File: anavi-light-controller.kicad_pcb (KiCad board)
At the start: 2 copper layers, 74.9 x 40.6 mm, 23 parts, among them J1 Screw_Terminal_1x04, P1 CONN_01X03, Q1 IRF8721PBF-1, Q2 IRF8721PBF-1, Q3 IRF8721PBF-1, SW1 SW_DIP_x01, U1 I2C_SENS_1, U2 I2C_SENS_1, U3 I2C_SENS_1

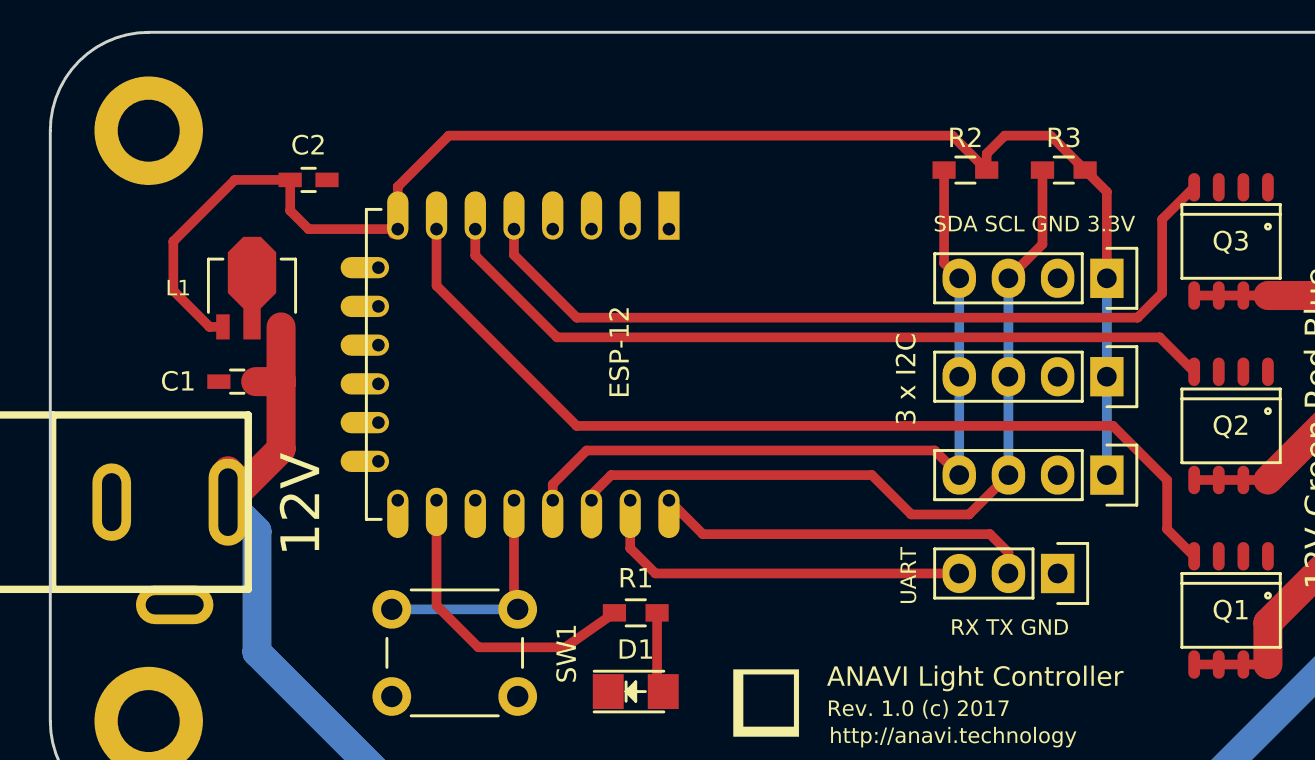
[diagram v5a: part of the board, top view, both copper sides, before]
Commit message: Change LDO voltage regulator
Use LD1117S33TR as LDO voltage regulator to drop
from 12V to 3.3V and to power the ESP8266 module.

Signed-off-by: Leon Anavi <leon@anavi.org>
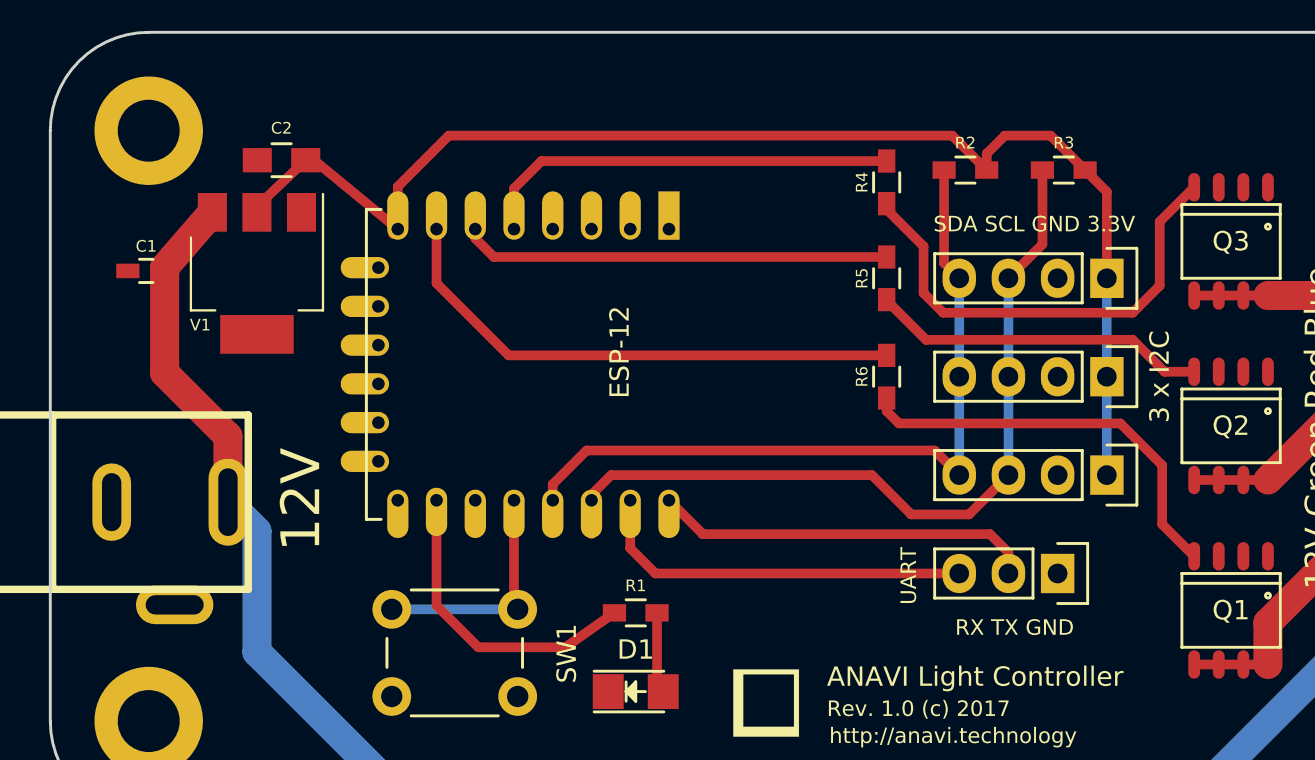
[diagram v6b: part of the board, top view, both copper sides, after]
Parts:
- removed L1: 78L33, smd-semi:SOT-89
- added R4: 220R, Resistors_SMD:R_0603_HandSoldering, F.Cu at (108.0, 78.9)
- added R5: 220R, Resistors_SMD:R_0603_HandSoldering, F.Cu at (108.0, 83.8)
- added R6: 220R, Resistors_SMD:R_0603_HandSoldering, F.Cu at (108.0, 88.9)
- added V1: LD1117S33TR, SOT-223, F.Cu at (75.4, 83.6)
- C1: value C -> 100nF
- C2: value C -> 10uF; footprint Capacitors_SMD:C_0603_HandSoldering -> Capacitors_SMD:C_0805_HandSoldering
- DC1: value 12V -> dc_jack
- moved C1 7.40 mm to (69.7, 83.4)
- moved C2 1.73 mm to (76.7, 77.7), turned to 180 degrees
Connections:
- Q1 pad 4: Net-(ESP-12-Pad7) -> Net-(Q1-Pad4)
- Q2 pad 4: Net-(ESP-12-Pad6) -> Net-(Q2-Pad4)
- Q3 pad 4: Net-(ESP-12-Pad5) -> Net-(Q3-Pad4)
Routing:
- net Net-(Q3-Pad4): track 0.00 -> 24.9 mm
- net Net-(Q1-Pad4): track 0.00 -> 21.9 mm
- net Net-(ESP-12-Pad7): track 49.3 -> 27.6 mm
- net Net-(ESP-12-Pad5): track 43.3 -> 21.9 mm
- net Net-(ESP-12-Pad6): track 41.1 -> 22.2 mm
- net Net-(Q2-Pad4): track 0.00 -> 17.6 mm
- net +3V3: track 79.3 -> 69.5 mm
- net +12V: track 91.6 -> 95.7 mm
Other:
- board text added: "12V"

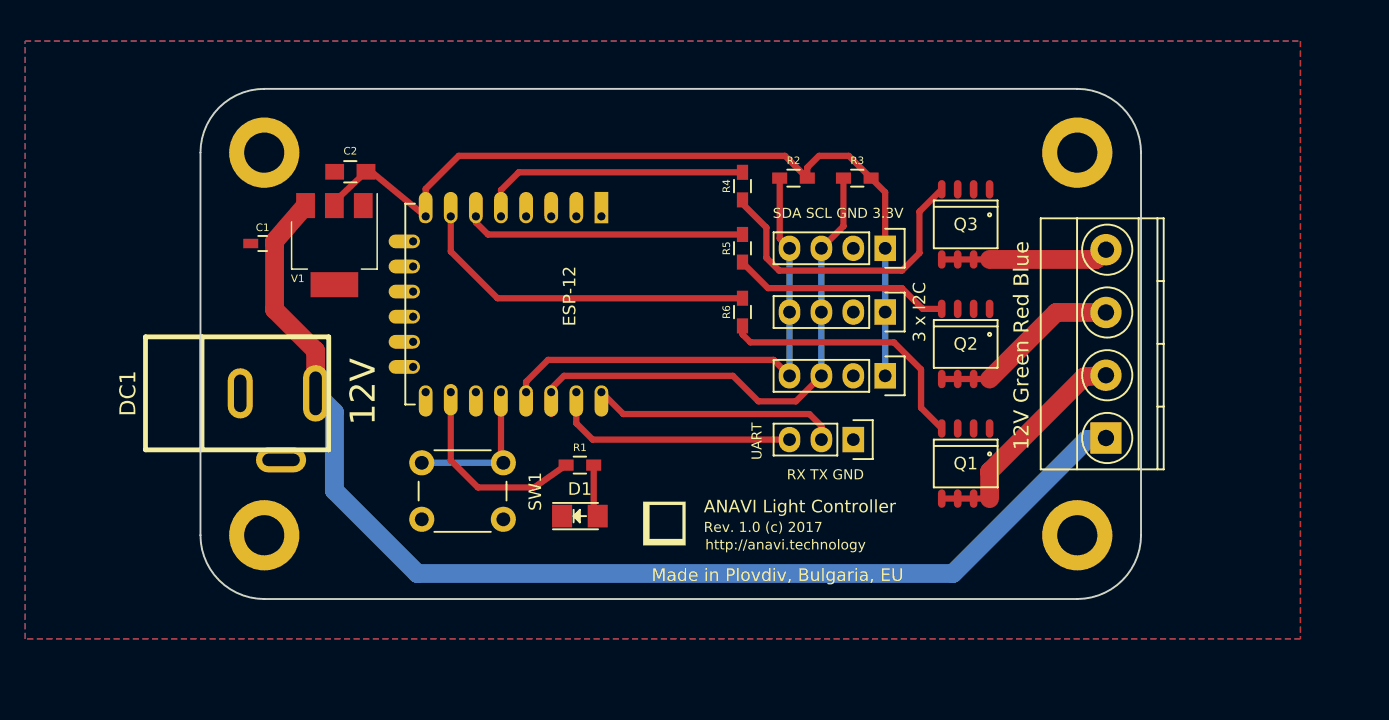
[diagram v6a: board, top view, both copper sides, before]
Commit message: Enable ESP-12; Fix the button and LED
Enable ESP-12 by connecting GPIO5 to GND and CH_PD
to 3.3V. Add 2K resistor to GPIO0 to fix the button
and move the alarm LED on the other side.

Signed-off-by: Leon Anavi <leon@anavi.org>
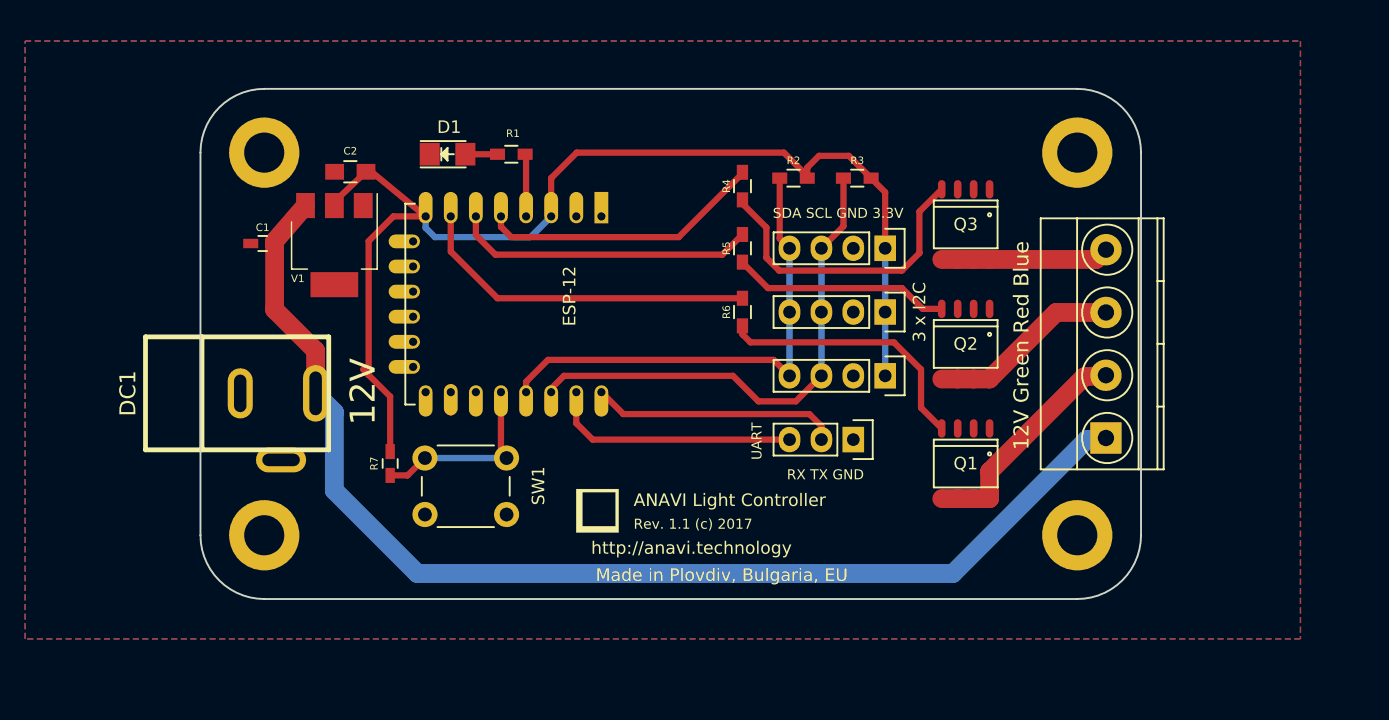
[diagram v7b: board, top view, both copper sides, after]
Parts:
- added R7: 2K, Capacitors_SMD:C_0603_HandSoldering, F.Cu at (79.9, 101.0)
- moved D1 30.7 mm to (84.5, 76.3)
- moved R1 25.4 mm to (89.5, 76.3), turned to 180 degrees
- moved G*** 5.43 mm to (96.4, 104.8)
- moved SW1 0.46 mm to (89.2, 105.0)
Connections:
- ESP-12 pad 10: Net-(ESP-12-Pad10) -> GND
- ESP-12 pad 3: (no net) -> +3V3
- ESP-12 pad 4: (no net) -> Net-(ESP-12-Pad4)
- R1 pad 1: Net-(ESP-12-Pad10) -> Net-(ESP-12-Pad4)
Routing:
- net +3V3: track 69.5 -> 95.7 mm
- net Net-(ESP-12-Pad10): track 19.3 -> 0.00 mm
- net Net-(ESP-12-Pad4): track 0.00 -> 4.98 mm
- net Net-(J1-Pad4): track 13.4 -> 17.2 mm
- net Net-(ESP-12-Pad12): track 12.5 -> 16.1 mm
- net GND: track 0.00 -> 3.24 mm
- net Net-(ESP-12-Pad6): track 22.2 -> 24.1 mm
- net Net-(D1-Pad2): track 4.20 -> 2.56 mm
- net Net-(ESP-12-Pad5): track 21.9 -> 22.6 mm
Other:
- board text added: "Rev. 1.1 (c) 2017"
- board text removed: "Rev. 1.0 (c) 2017"

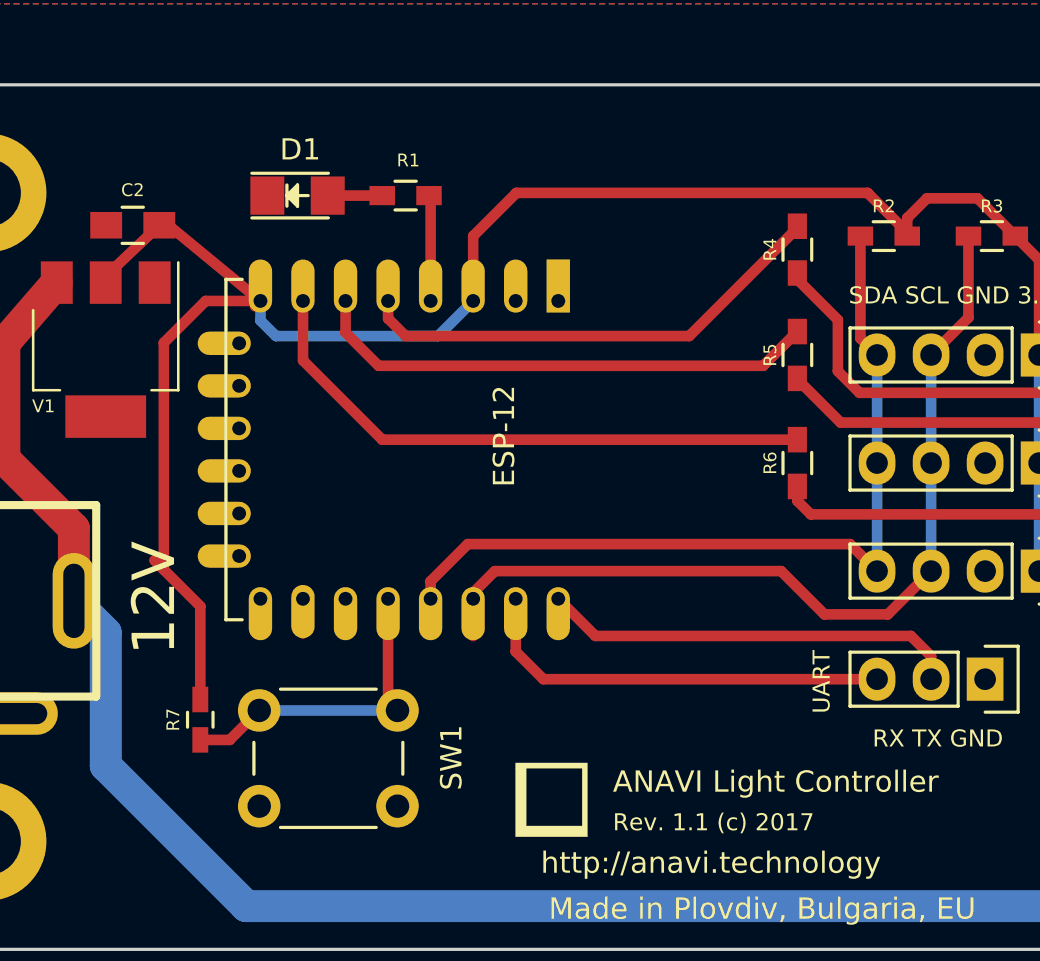
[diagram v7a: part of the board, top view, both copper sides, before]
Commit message: kicad_pcb: Adjust positions of components
Adjust the positions of the red LED and the button.

Signed-off-by: Leon Anavi <leon@anavi.org>
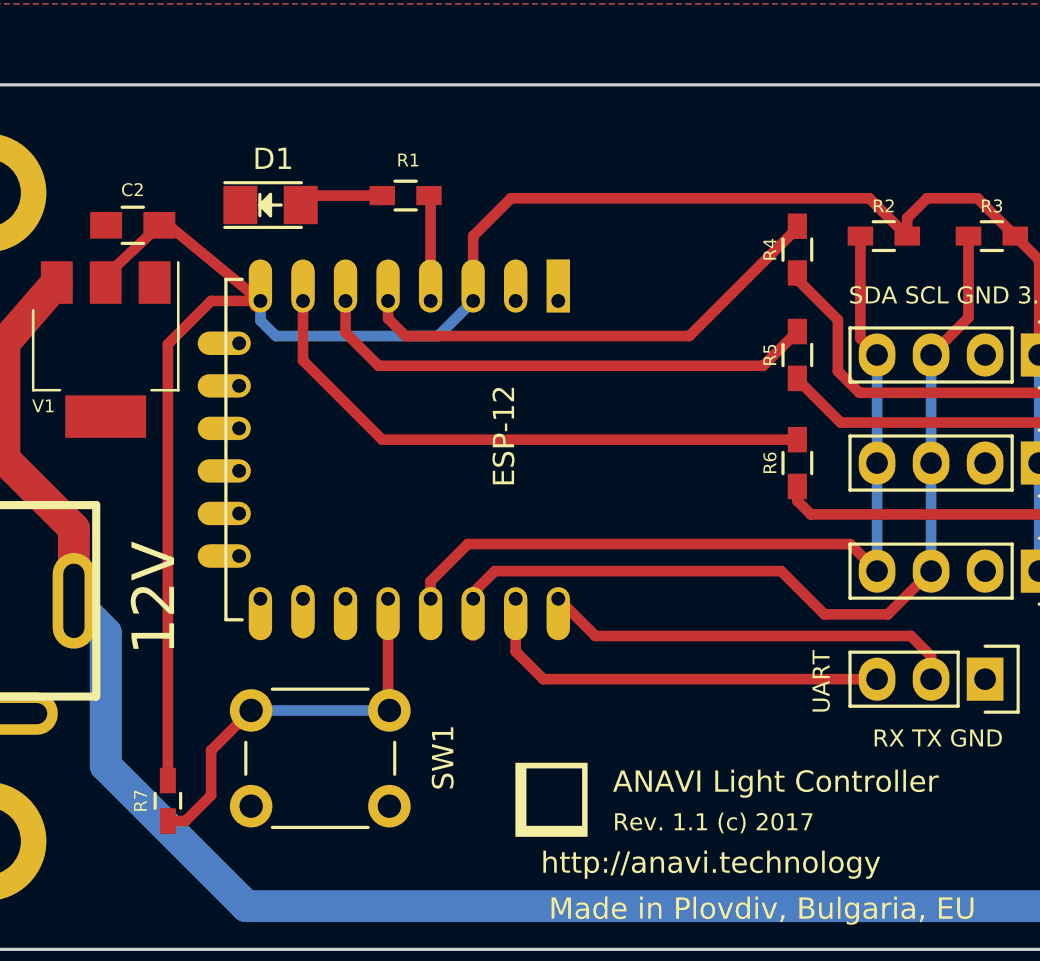
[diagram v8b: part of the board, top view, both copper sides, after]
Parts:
- moved R7 4.10 mm to (78.4, 104.8)
- moved D1 1.35 mm to (83.2, 76.8)
- moved SW1 0.38 mm to (88.8, 105.0)
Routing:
- net Net-(ESP-12-Pad12): track 16.1 -> 20.5 mm
- net +3V3: track 95.7 -> 97.8 mm
- net Net-(D1-Pad2): track 2.56 -> 4.55 mm
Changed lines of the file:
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@@
     (links 67)
     (no_connects 0)
-    (area 64.694999 71.044999 139.775001 111.835001)
+    (area 50.8 67.31 152.400001 114.935001)
     (thickness 1.6)
     (drawings 18)
-    (tracks 142)
+    (tracks 144)
     (zones 0)
     (modules 27)
@@
       (drillshape 0)
       (scaleselection 1)
-      (outputdirectory plots/anavi-light-controller-r1.0/))
+      (outputdirectory plots/anavi-light-controller-r1.1/))
   )
   (net 0 "")
@@
   )
   (module LEDs:LED_1206 (layer F.Cu)
-    (at 84.455 76.327)
+    (at 83.185 76.7715)
     (descr "LED 1206 smd package")
     (tags "LED1206 SMD")
@@
   )
   (module Buttons_Switches_ThroughHole:SW_PUSH_6mm_h4.3mm (layer F.Cu)
-    (at 89.154 105.029 180)
+    (at 88.773 105.029 180)
     (descr "tactile push button, 6x6mm e.g. PHAP33xx series, height=4.3mm")
     (tags "tact sw push 6mm")
@@
   )
   (module Capacitors_SMD:C_0603_HandSoldering (layer F.Cu)
-    (at 79.883 100.965 90)
+    (at 78.359 104.775 90)
     (descr "Capacitor SMD 0603, hand soldering")
     (tags "capacitor 0603")
@@
     (effects (font (size 1 1) (thickness 0.2)))
   )
-  (segment (start 88.435 76.327) (end 85.87486 76.327) (width 0.5) (layer F.Cu) (net 1))
+  (segment (start 88.435 76.327) (end 85.04936 76.327) (width 0.5) (layer F.Cu) (net 1))
+  (segment (start 85.04936 76.327) (end 84.60486 76.7715) (width 0.5) (layer F.Cu) (net 1))
+  (segment (start 84.98586 76.3905) (end 84.60486 76.7715) (width 0.5) (layer F.Cu) (net 1) (status 30))
   (segment (start 84.7105 95.28) (end 84.7105 96.8995) (width 0.5) (layer F.Cu) (net 2))
   (segment (start 84.7105 95.28) (end 84.7105 96.9025) (width 0.5) (layer F.Cu) (net 2))
@@
   (segment (start 135.175 94.06) (end 136.906 93.933) (width 1.5) (layer F.Cu) (net 5) (status 20))
   (segment (start 127.635 101.6) (end 135.175 94.06) (width 1.5) (layer F.Cu) (net 5))
-  (segment (start 78.1685 93.9165) (end 78.1685 83.2485) (width 0.5) (layer F.Cu) (net 6))
-  (segment (start 80.137 81.28) (end 82.7105 81.28) (width 0.5) (layer F.Cu) (net 6))
-  (segment (start 78.1685 83.2485) (end 80.137 81.28) (width 0.5) (layer F.Cu) (net 6))
-  (segment (start 79.883 100.015) (end 79.883 95.631) (width 0.5) (layer F.Cu) (net 6) (status 10))
-  (segment (start 79.883 95.631) (end 78.1685 93.9165) (width 0.5) (layer F.Cu) (net 6))
-  (segment (start 78.1685 93.9165) (end 77.724 93.472) (width 0.5) (layer F.Cu) (net 6))
+  (segment (start 92.7105 81.28) (end 92.7105 78.2315) (width 0.5) (layer F.Cu) (net 6))
+  (segment (start 111.336 76.454) (end 113.114 78.232) (width 0.5) (layer F.Cu) (net 6))
+  (segment (start 94.488 76.454) (end 111.336 76.454) (width 0.5) (layer F.Cu) (net 6))
+  (segment (start 92.7105 78.2315) (end 94.488 76.454) (width 0.5) (layer F.Cu) (net 6))
+  (segment (start 78.359 103.825) (end 78.359 83.312) (width 0.5) (layer F.Cu) (net 6))
+  (segment (start 80.391 81.28) (end 82.7105 81.28) (width 0.5) (layer F.Cu) (net 6))
+  (segment (start 78.359 83.312) (end 80.391 81.28) (width 0.5) (layer F.Cu) (net 6))
   (segment (start 75.438 80.416) (end 75.438 79.863) (width 0.5) (layer F.Cu) (net 6) (status 30))
   (segment (start 75.438 80.416) (end 75.438 79.817) (width 0.5) (layer F.Cu) (net 6) (status 30))
@@
   (segment (start 77.958 77.724) (end 78.3925 77.724) (width 0.5) (layer F.Cu) (net 6) (status 30))
   (segment (start 113.114 78.232) (end 113.114 78.062) (width 0.5) (layer F.Cu) (net 6))
-  (segment (start 113.114 78.062) (end 111.252 76.2) (width 0.5) (layer F.Cu) (net 6))
-  (segment (start 92.7105 78.2315) (end 92.7105 81.28) (width 0.5) (layer F.Cu) (net 6))
-  (segment (start 94.742 76.2) (end 92.7105 78.2315) (width 0.5) (layer F.Cu) (net 6))
-  (segment (start 111.252 76.2) (end 94.742 76.2) (width 0.5) (layer F.Cu) (net 6))
   (segment (start 82.7105 81.28) (end 82.7105 82.2025) (width 0.5) (layer B.Cu) (net 6))
   (segment (start 82.7105 82.2025) (end 83.439 82.931) (width 0.5) (layer B.Cu) (net 6))
@@
   (segment (start 91.0595 82.931) (end 92.7105 81.28) (width 0.5) (layer B.Cu) (net 6))
   (segment (start 113.114 78.232) (end 113.114 77.386) (width 0.5) (layer F.Cu) (net 6))
+  (segment (start 113.114 77.386) (end 114.046 76.454) (width 0.5) (layer F.Cu) (net 6))
+  (segment (start 114.046 76.454) (end 116.416 76.454) (width 0.5) (layer F.Cu) (net 6))
   (segment (start 116.416 76.454) (end 118.194 78.232) (width 0.5) (layer F.Cu) (net 6))
-  (segment (start 114.046 76.454) (end 116.416 76.454) (width 0.5) (layer F.Cu) (net 6))
-  (segment (start 113.114 77.386) (end 114.046 76.454) (width 0.5) (layer F.Cu) (net 6))
   (segment (start 119.3165 83.82) (end 119.3165 79.3545) (width 0.5) (layer F.Cu) (net 6))
   (segment (start 119.3165 79.3545) (end 118.194 78.232) (width 0.5) (layer F.Cu) (net 6))
@@
   (segment (start 90.7105 81.28) (end 90.7105 76.4025) (width 0.5) (layer F.Cu) (net 18))
   (segment (start 90.7105 76.4025) (end 90.635 76.327) (width 0.5) (layer F.Cu) (net 18))
-  (segment (start 79.883 101.915) (end 81.268 101.915) (width 0.5) (layer F.Cu) (net 19))
-  (segment (start 81.268 101.915) (end 82.654 100.529) (width 0.5) (layer F.Cu) (net 19))
-  (segment (start 88.7105 95.28) (end 88.7105 100.0855) (width 0.5) (layer F.Cu) (net 19))
-  (segment (start 88.7105 100.0855) (end 89.154 100.529) (width 0.5) (layer F.Cu) (net 19))
-  (segment (start 88.9645 100.3395) (end 89.154 100.529) (width 0.5) (layer F.Cu) (net 19) (status 30))
-  (segment (start 89.154 100.529) (end 82.654 100.529) (width 0.5) (layer B.Cu) (net 19) (status 30))
-  (segment (start 88.9645 100.3395) (end 89.154 100.529) (width 0.5) (layer F.Cu) (net 19) (status 30))
-  (segment (start 88.9645 100.3395) (end 89.154 100.529) (width 0.5) (layer F.Cu) (net 19) (status 30))
+  (segment (start 78.359 105.725) (end 79.187 105.725) (width 0.5) (layer F.Cu) (net 19))
+  (segment (start 80.391 102.411) (end 82.273 100.529) (width 0.5) (layer F.Cu) (net 19))
+  (segment (start 80.391 104.521) (end 80.391 102.411) (width 0.5) (layer F.Cu) (net 19))
+  (segment (start 79.187 105.725) (end 80.391 104.521) (width 0.5) (layer F.Cu) (net 19))
+  (segment (start 88.7105 95.28) (end 88.7105 100.4665) (width 0.5) (layer F.Cu) (net 19))
+  (segment (start 88.7105 100.4665) (end 88.773 100.529) (width 0.5) (layer F.Cu) (net 19))
+  (segment (start 88.3295 100.0855) (end 88.773 100.529) (width 0.5) (layer F.Cu) (net 19) (status 30))
+  (segment (start 88.5835 100.3395) (end 88.773 100.529) (width 0.5) (layer F.Cu) (net 19) (status 30))
+  (segment (start 88.773 100.529) (end 82.273 100.529) (width 0.5) (layer B.Cu) (net 19) (status 30))
+  (segment (start 88.5835 100.3395) (end 88.773 100.529) (width 0.5) (layer F.Cu) (net 19) (status 30))
+  (segment (start 88.5835 100.3395) (end 88.773 100.529) (width 0.5) (layer F.Cu) (net 19) (status 30))
   (zone (net 2) (net_name GND) (layer F.Cu) (hatch edge 0.508)
     (connect_pads (clearance 0.508))
